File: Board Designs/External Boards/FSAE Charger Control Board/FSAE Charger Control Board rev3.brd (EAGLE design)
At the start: 67.8 x 86.5 mm, 38 parts, among them X1 CONNECTOR-4, X2 CONNECTOR-12

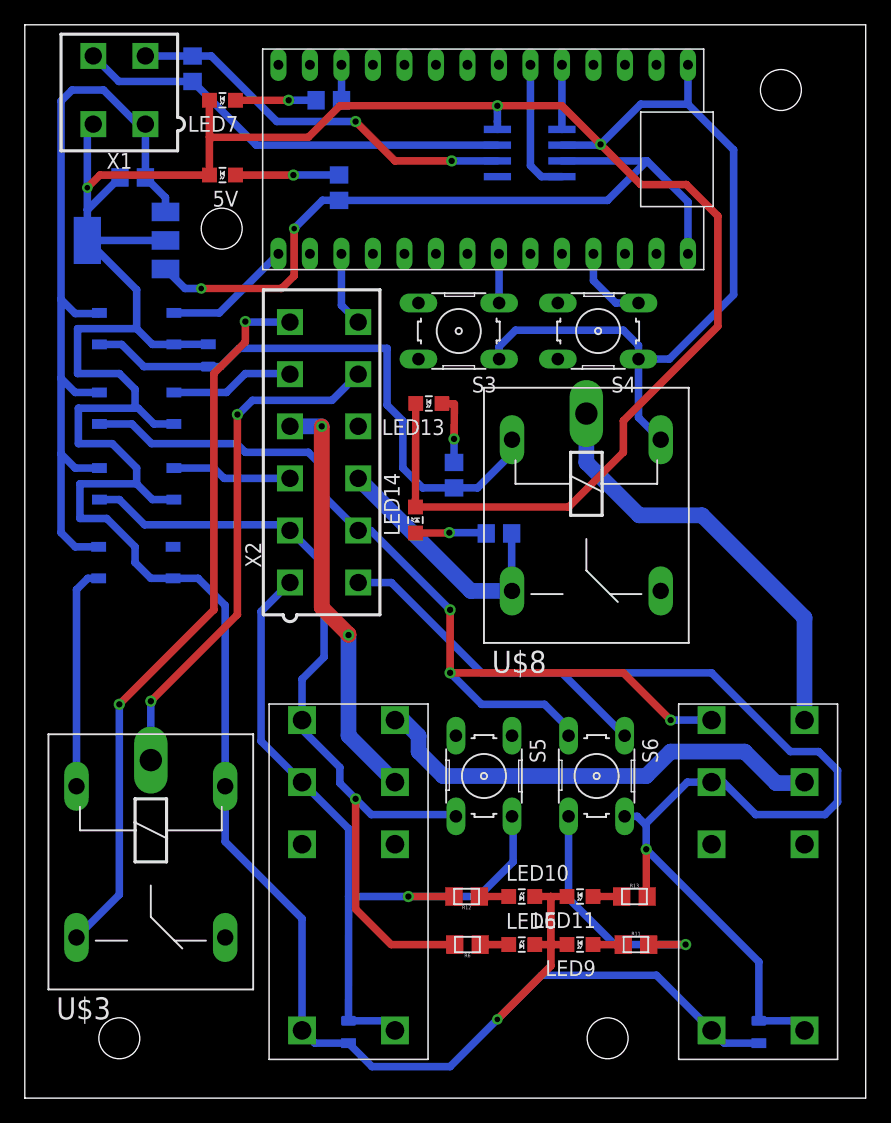
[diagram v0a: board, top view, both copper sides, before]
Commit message: Update board silkscreens for manufacture, add FH AMS Test Port to BMS layout
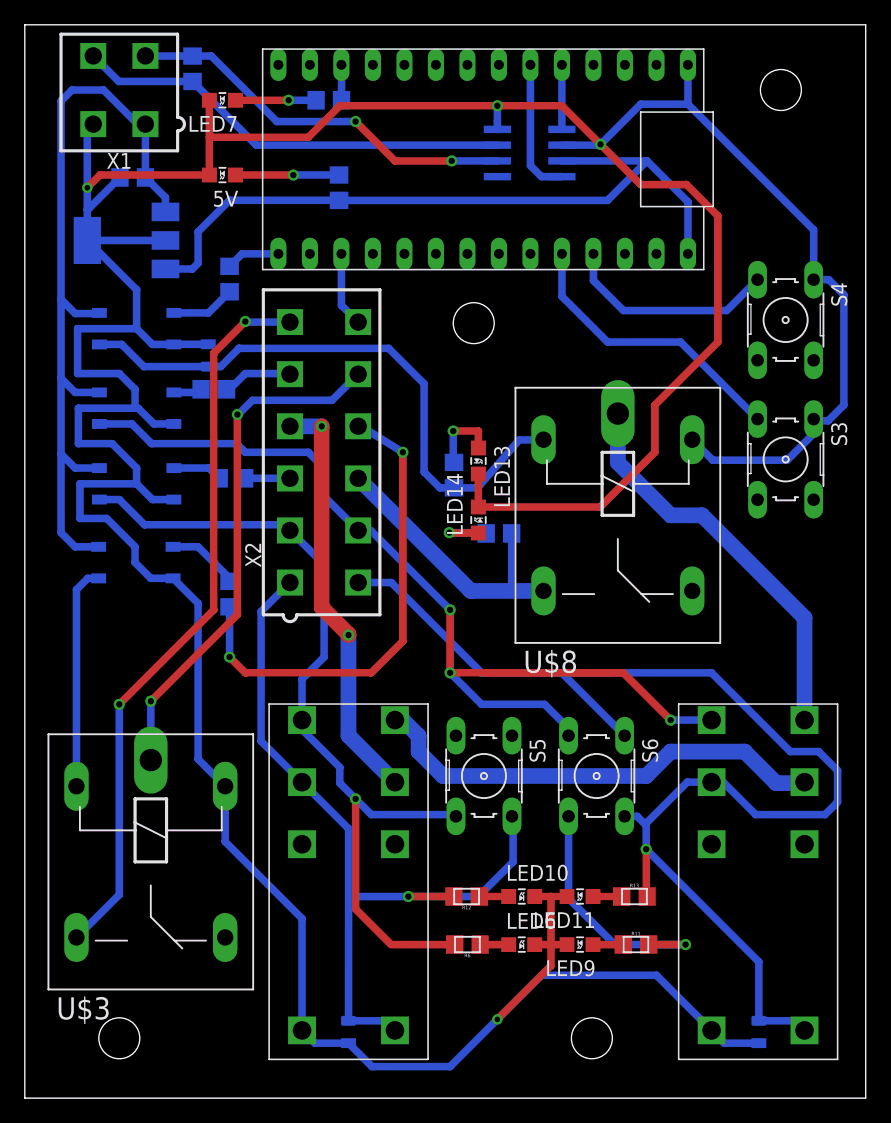
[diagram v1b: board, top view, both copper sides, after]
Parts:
- added R2, R3, R4, R5: (no value), HyTechDevices:0805
- moved S3 28.3 mm to (61.3, 51.5), turned to 270 degrees
- moved S4 15.1 mm to (61.3, 62.7), turned to 270 degrees
- moved LED13 6.12 mm to (36.6, 51.4), turned to 180 degrees
- moved LED14 5.08 mm to (36.6, 46.6)
- moved U$8 2.54 mm to (38.9, 57.1)
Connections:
- removed net BMS: BMS_SSR1.1, X2.5
- removed net IMD: IMD_SSR1.1, X2.3
- new net N$11: BMS_SSR1.1, R3.2
- new net N$15: R2.1, X2.3
- new net N$16: R3.1, X2.5
- new net N$17: R5.2, SOFT_SSR1.1
- new net N$18: R4.1, U$1.D13
- new net N$4: IMD_SSR1.1, R2.2
- net BMS_INRLK: now also R5.1, X2.10; no longer SOFT_SSR1.1
- net BTN_Y: now also U$1.A8; no longer U$1.A6
- net SW_KILL: now also R4.2; no longer U$1.D13
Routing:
- net BMS_INRLK: track 0.00 -> 39.0 mm, vias 0 -> 2
- net BTN_Y: track 3.97 -> 23.3 mm
- net GND: track 367.3 -> 354.2 mm
- net BTN_X: track 6.54 -> 17.4 mm
- net BMS: track 10.0 -> 0.00 mm
- net IMD: track 9.71 -> 0.00 mm
- net N$17: track 0.00 -> 5.85 mm
- net N$16: track 0.00 -> 5.66 mm
- net SW_KILL: track 10.4 -> 5.20 mm
- net SHUTDOWN_OUT: track 20.8 -> 25.9 mm
- net N$18: track 0.00 -> 4.35 mm
- net N$4: track 0.00 -> 4.00 mm
- net N$15: track 0.00 -> 3.66 mm
- net SHUTDOWN_IN_B: track 35.0 -> 32.4 mm
- net N$11: track 0.00 -> 2.30 mm
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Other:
- board text added: "BMS12"
- board text added: "BMSR"
- board text added: "IMD12"
- board text added: "IMDR"
- board text added: "SDOUT"
- board text added: "SWKILL"
- board text added: "fsae_charger_control_board_rev3 Designed by Chad Hendrix"
- board text removed: "Georgia Tech HyTech Racing 2018 FSAE Charger Control Board rev2 Designed by Chad Hendrix"
- board text removed: "LED A"
- board text removed: "LED B"
- board text removed: "LED C"
- board text removed: "LED D"
